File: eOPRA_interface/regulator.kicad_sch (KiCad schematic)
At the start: 21 parts, among them U14 AP2205-50, U34 AP2213-8_SOIC

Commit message: initial state
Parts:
- D1, D2: PN 3,2 -> 3,6
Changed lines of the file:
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@@
       (effects (font (size 1.27 1.27)) hide)
     )
-    (property "PN" "3,2" (at 53.34 80.01 0)
+    (property "PN" "3,6" (at 53.34 80.01 0)
       (effects (font (size 1.27 1.27)) hide)
     )
@@
       (effects (font (size 1.27 1.27)) hide)
     )
-    (property "PN" "3,2" (at 53.34 76.2 0)
-      (effects (font (size 1.27 1.27)) hide)
-    )
+    (property "PN" "3,6" (at 53.34 76.2 0)
+      (effects (font (size 1.27 1.27)) hide)
+    )

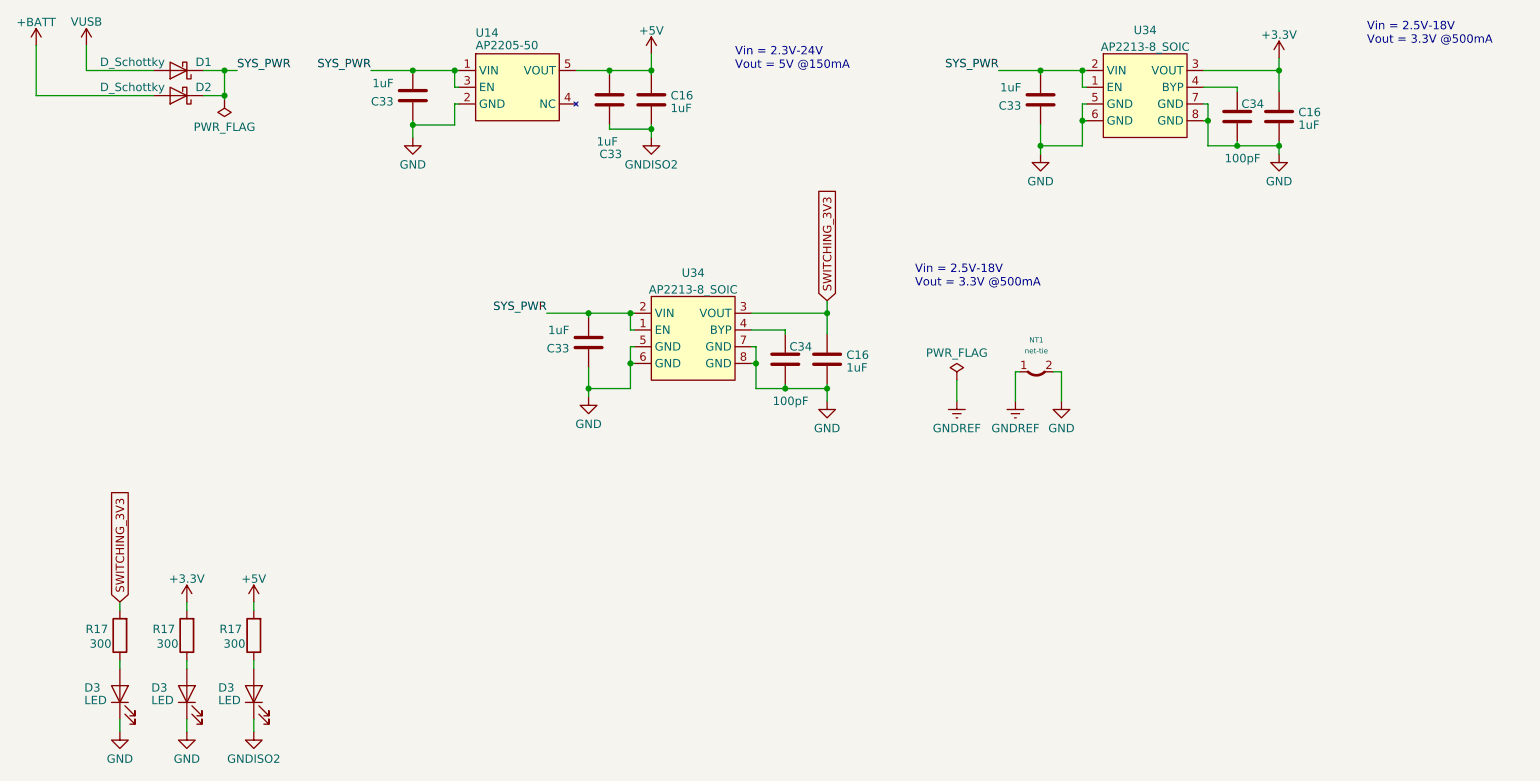
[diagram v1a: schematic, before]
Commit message: switch port on interrupt
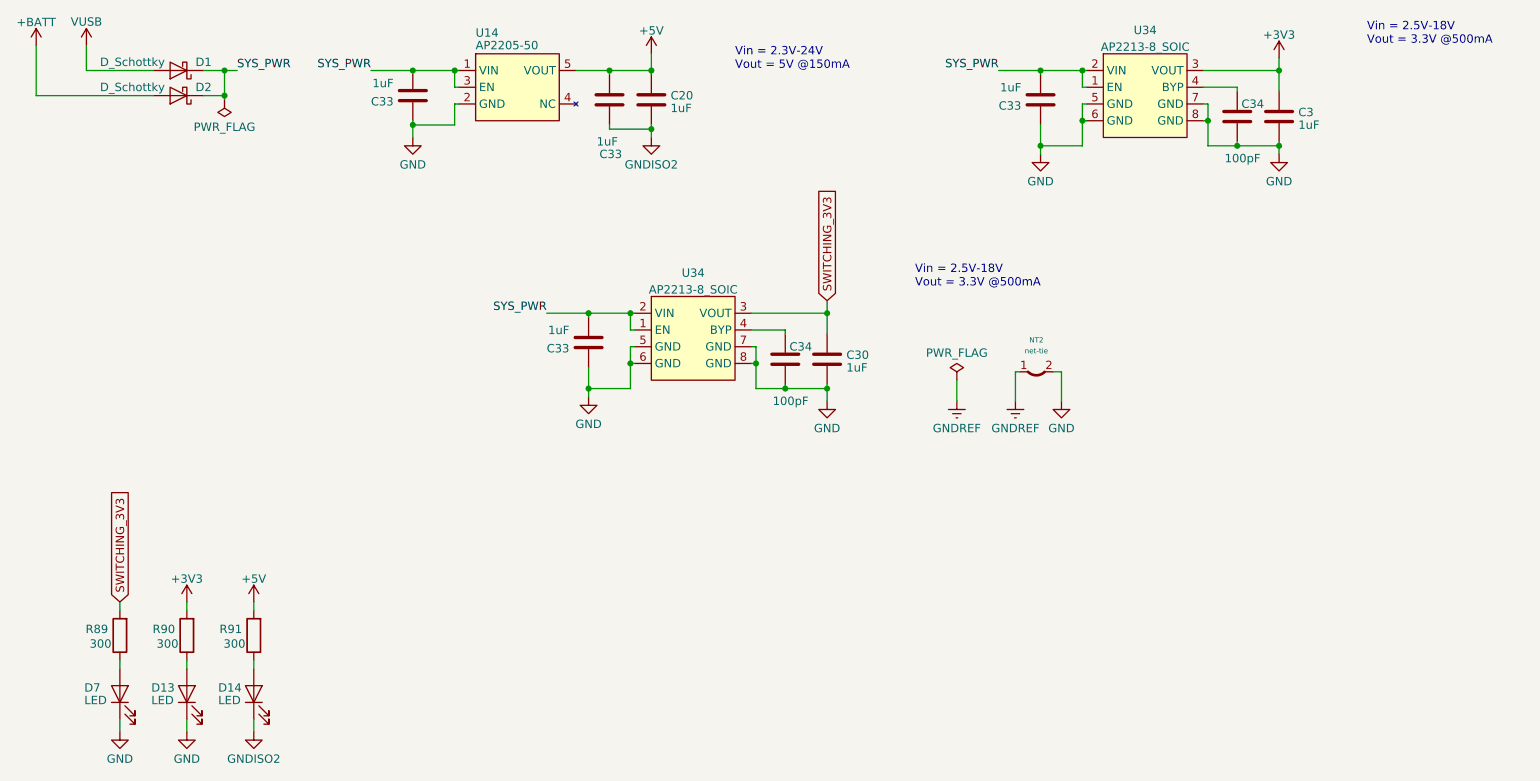
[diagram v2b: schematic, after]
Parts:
- renumbered C16 to C20, C16 to C3, C16 to C30, D3 to D13, D3 to D14, D3 to D7, NT1 to NT2, R17 to R89, R17 to R90, R17 to R91
